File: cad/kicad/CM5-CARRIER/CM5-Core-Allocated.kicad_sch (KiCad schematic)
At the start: 7 parts, among them J501 RADXA CM5 U13-A MATE, J502 RADXA CM5 U13-B MATE, J503 RADXA CM5 J1 MATE, J510 CM5_POWER_SERVICE, J511 DEBUG_UART_3V3, J512 INTERNAL_USB_RECOVERY, J513 CM5_POWER_ENTRY

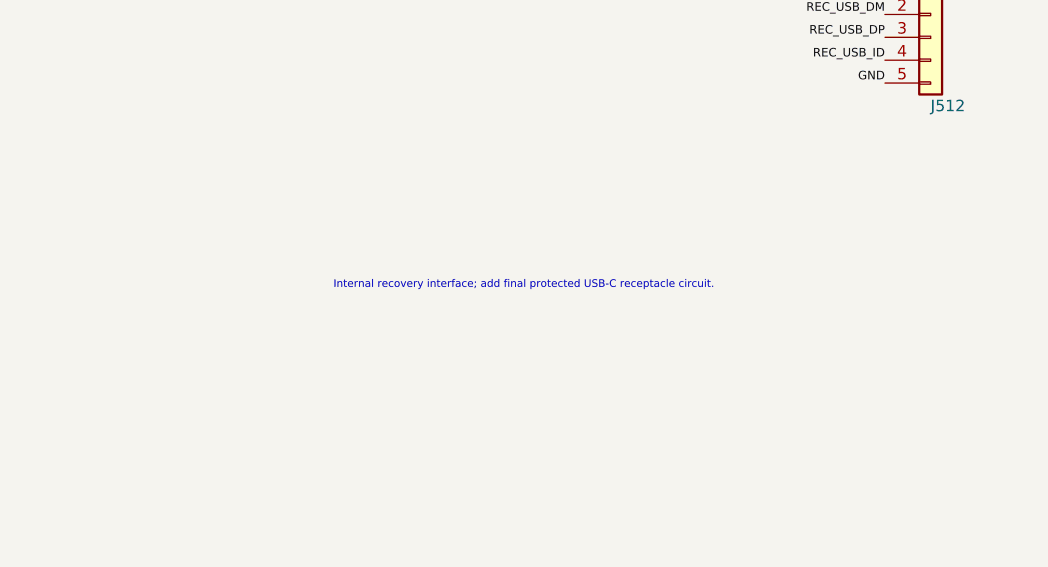
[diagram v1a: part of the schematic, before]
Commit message: Complete A1 detailed carrier and audio capture
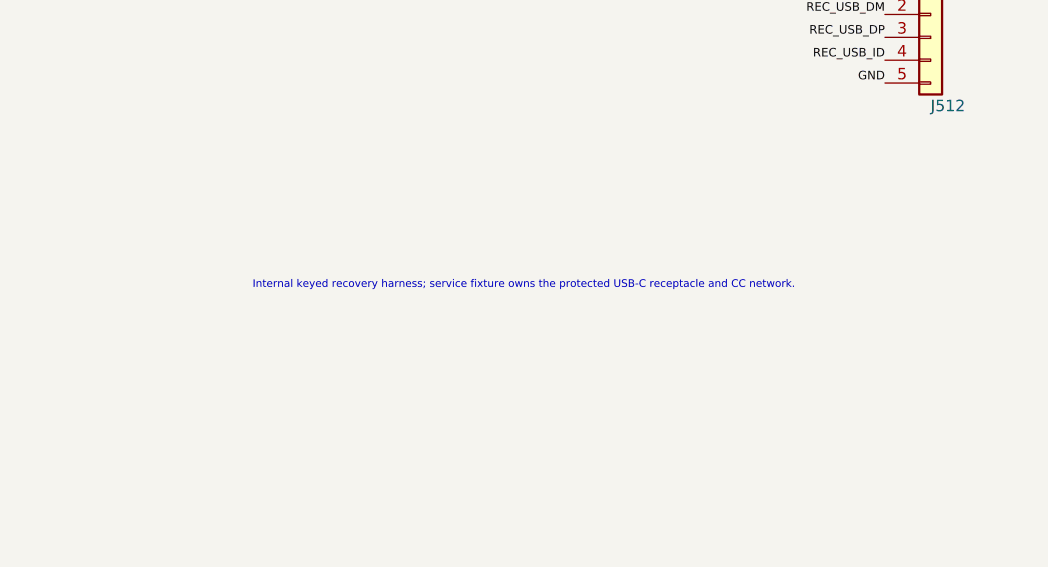
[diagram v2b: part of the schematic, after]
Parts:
- J510: footprint (none) -> Connector_JST:JST_GH_BM06B-GHS-TBT_1x06-1MP_P1.25mm_Vertical; MPN (none) -> BM06B-GHS-TBT(LF)(SN); Manufacturer (none) -> JST
- J511: footprint (none) -> Connector_JST:JST_GH_BM04B-GHS-TBT_1x04-1MP_P1.25mm_Vertical; MPN (none) -> BM04B-GHS-TBT(LF)(SN); Manufacturer (none) -> JST
- J512: footprint (none) -> Connector_JST:JST_GH_BM05B-GHS-TBT_1x05-1MP_P1.25mm_Vertical; MPN (none) -> BM05B-GHS-TBT(LF)(SN); Manufacturer (none) -> JST
- J513: footprint (none) -> Connector_Molex:Molex_Micro-Fit_3.0_43045-0812_2x04_P3.00mm_Vertical; MPN (none) -> 43045-0812; Manufacturer (none) -> Molex
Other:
- note added: "Internal keyed recovery harness; service fixture owns the protected USB-C receptacle and CC network."
- note removed: "Internal recovery interface; add final protected USB-C receptacle circuit."
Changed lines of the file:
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@@
+			)
+		)
+		(property "Footprint" "Connector_JST:JST_GH_BM06B-GHS-TBT_1x06-1MP_P1.25mm_Vertical"
+			(at 90.17 234.95 0.0000)
+			(effects
+				(font
+					(size 1.27 1.27)
+				)
+				(hide yes)
+			)
+		)
+		(property "Manufacturer" "JST"
+			(at 92.71 240.0299 0)
+			(effects
+				(font
+					(size 1.27 1.27)
+				)
+				(hide yes)
+			)
+		)
+		(property "MPN" "BM06B-GHS-TBT(LF)(SN)"
+			(at 92.71 240.0299 0)
+			(effects
+				(font
+					(size 1.27 1.27)
+				)
+				(hide yes)
 			)
 		)
@@
 			)
 		)
+		(property "Footprint" "Connector_JST:JST_GH_BM04B-GHS-TBT_1x04-1MP_P1.25mm_Vertical"
+			(at 214.63 232.41 0.0000)
+			(effects
+				(font
+					(size 1.27 1.27)
+				)
+				(hide yes)
+			)
+		)
+		(property "Manufacturer" "JST"
+			(at 217.17 237.4899 0)
+			(effects
+				(font
+					(size 1.27 1.27)
+				)
+				(hide yes)
+			)
+		)
+		(property "MPN" "BM04B-GHS-TBT(LF)(SN)"
+			(at 217.17 237.4899 0)
+			(effects
+				(font
+					(size 1.27 1.27)
+				)
+				(hide yes)
+			)
+		)
 		(pin "1"
 		)
@@
 			)
 		)
+		(property "Footprint" "Connector_JST:JST_GH_BM05B-GHS-TBT_1x05-1MP_P1.25mm_Vertical"
+			(at 330.2 232.41 0.0000)
+			(effects
+				(font
+					(size 1.27 1.27)
+				)
+				(hide yes)
+			)
+		)
+		(property "Manufacturer" "JST"
+			(at 332.74 237.4899 0)
+			(effects
+				(font
+					(size 1.27 1.27)
+				)
+				(hide yes)
+			)
+		)
+		(property "MPN" "BM05B-GHS-TBT(LF)(SN)"
+			(at 332.74 237.4899 0)
+			(effects
+				(font
+					(size 1.27 1.27)
+				)
+				(hide yes)
+			)
+		)
 		(pin "1"
 		)
@@
 			)
 		)
+		(property "Footprint" "Connector_Molex:Molex_Micro-Fit_3.0_43045-0812_2x04_P3.00mm_Vertical"
+			(at 469.9 232.41 0.0000)
+			(effects
+				(font
+					(size 1.27 1.27)
+				)
+				(hide yes)
+			)
+		)
+		(property "Manufacturer" "Molex"
+			(at 472.44 237.4899 0)
+			(effects
+				(font
+					(size 1.27 1.27)
+				)
+				(hide yes)
+			)
+		)
+		(property "MPN" "43045-0812"
+			(at 472.44 237.4899 0)
+			(effects
+				(font
+					(size 1.27 1.27)
+				)
+				(hide yes)
+			)
+		)
 		(pin "1"
 		)
@@
 		)
 	)
-	(text "Internal recovery interface; add final protected USB-C receptacle circuit."
+	(text "Internal keyed recovery harness; service fixture owns the protected USB-C receptacle and CC network."
 		(exclude_from_sim no)
 		(at 285 260 0.0000)

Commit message: Lock CM5 power and radio interfaces before routing
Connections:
- net HDMI_5V_OPTION renamed IO_5V0
- net SYS_5V15 renamed SYS_4V0
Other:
- note added: "Kelvin-sense SYS_4V0 at J501; 4.0 V follows the Radxa CM5 carrier design note."
- note added: "Pins 145/147 remain HDMI HEAC reserved. U13-B pin 106 receives the dedicated IO_5V0 rail."
- note removed: "Kelvin-sense SYS_5V15 at J501; final setpoint remains a release gate."
- note removed: "Pins 145/147 remain HDMI HEAC reserved. HDMI_5V_OPTION remains a controlled DNP/link decision."
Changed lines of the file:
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@@
 		)
 	)
-	(label "SYS_5V15"
+	(label "SYS_4V0"
 		(at 77.47 139.7 0.0000)
 		(effects
@@
 		)
 	)
-	(label "SYS_5V15"
+	(label "SYS_4V0"
 		(at 77.47 142.24 0.0000)
 		(effects
@@
 		)
 	)
-	(label "SYS_5V15"
+	(label "SYS_4V0"
 		(at 77.47 144.78 0.0000)
 		(effects
@@
 		)
 	)
-	(label "SYS_5V15"
+	(label "SYS_4V0"
 		(at 77.47 147.32 0.0000)
 		(effects
@@
 		)
 	)
-	(label "SYS_5V15"
+	(label "SYS_4V0"
 		(at 77.47 149.86 0.0000)
 		(effects
@@
 		)
 	)
-	(label "SYS_5V15"
+	(label "SYS_4V0"
 		(at 77.47 152.4 0.0000)
 		(effects
@@
 		)
 	)
-	(label "HDMI_5V_OPTION"
+	(label "IO_5V0"
 		(at 322.58 48.26 0.0000)
 		(effects
@@
 		)
 	)
-	(label "SYS_5V15"
+	(label "SYS_4V0"
 		(at 464.82 229.87 0.0000)
 		(effects
@@
 		)
 	)
-	(label "SYS_5V15"
+	(label "SYS_4V0"
 		(at 477.52 229.87 0.0000)
 		(effects
@@
 		)
 	)
-	(label "SYS_5V15"
+	(label "SYS_4V0"
 		(at 464.82 232.41 0.0000)
 		(effects
@@
 		)
 	)
-	(label "SYS_5V15"
+	(label "SYS_4V0"
 		(at 477.52 232.41 0.0000)
 		(effects
@@
 		)
 	)
-	(text "Kelvin-sense SYS_5V15 at J501; final setpoint remains a release gate."
+	(text "Kelvin-sense SYS_4V0 at J501; 4.0 V follows the Radxa CM5 carrier design note."
 		(exclude_from_sim no)
 		(at 420 260 0.0000)
@@
 		)
 	)
-	(text "Pins 145/147 remain HDMI HEAC reserved. HDMI_5V_OPTION remains a controlled DNP/link decision."
+	(text "Pins 145/147 remain HDMI HEAC reserved. U13-B pin 106 receives the dedicated IO_5V0 rail."
 		(exclude_from_sim no)
 		(at 45 348 0.0000)

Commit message: Audit schematic logic against controlled datasheets
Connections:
- net HDMI_HEAC_N: no longer names the net of J502.147 (HDMI0_TX_SBDN)
- net PCIE_UP_PERST_N renamed PCIE_UP_PERST_CMD_N
- net WAN1_LED2: no longer names the net of J501.15 (PHY1_LED2_Y)
- no-connect marks 148 -> 150
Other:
- note added: "76 / 76 contacts owned; 74 connected, 2 assigned NC, 0 duplicate physical-pin claims."
- note added: "Pin 145 reaches HDMI pin 14; pin 147 is assigned NC because HEAC/ARC is unused. U13-B pin 106 receives IO_5V0."
- note removed: "76 / 76 allocated contacts connected; 0 duplicate physical-pin claims."
- note removed: "Pins 145/147 remain HDMI HEAC reserved. U13-B pin 106 receives the dedicated IO_5V0 rail."

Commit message: Lock source-verified PCB mating geometry
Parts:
- J501: footprint Connector_Hirose_DF40:Hirose_DF40C-100DS-0.4V_2x50_P0.4mm -> CM5Carrier:Radxa_CM5_U33A_DF40C_100DS_OFFICIAL
- J502: footprint Connector_Hirose_DF40:Hirose_DF40C-100DS-0.4V_2x50_P0.4mm -> CM5Carrier:Radxa_CM5_U33B_DF40C_100DS_OFFICIAL
- J503: footprint Connector_Hirose_DF40:Hirose_DF40C-100DS-0.4V_2x50_P0.4mm -> CM5Carrier:Radxa_CM5_J24_DF40C_100DS_OFFICIAL
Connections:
- net GND: now also J501.201 (MODULE_MOUNT_GND_1), J501.202 (MODULE_MOUNT_GND_2), J501.203 (MODULE_MOUNT_GND_3), J501.204 (MODULE_MOUNT_GND_4)
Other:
- note added: "PCB lock: J501 and J502 share the U33 origin; J503 is +11.405, -25.415 mm at -90 degrees."
- note added: "U13-A: 100 contacts + official grounded module pads 201-204"
- note removed: "U13-A: 100 physical contacts"
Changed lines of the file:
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@@
 		(rev "A1")
 		(company "ProComm")
-		(comment 1 "Three 100-contact Hirose DF40C mates; all physical pin numbers follow CM5 V2.21")
+		(comment 1 "Three DF40C-100DS mates; pad geometry and relative placement come from Radxa IO V2.20")
 		(comment 2 "76 contacts are owned: 74 connected and 2 assigned no-connect; all other functions are no-connect")
-		(comment 3 "All connector grounds join the carrier ground plane; allocated GPIO domain is 3.3 V")
+		(comment 3 "U33-A includes the four official grounded CM5 mounting pads; allocated GPIO domain is 3.3 V")
 		(comment 4 "DETAILED CAPTURE BASELINE - verify CM5 voltage limits before release")
 	)
@@
 			)
 		)
-		(property "Footprint" "Connector_Hirose_DF40:Hirose_DF40C-100DS-0.4V_2x50_P0.4mm"
+		(property "Footprint" "CM5Carrier:Radxa_CM5_U33A_DF40C_100DS_OFFICIAL"
 			(at 105.41 105.41 0.0000)
 			(effects
@@
 		(pin "100"
 		)
+		(pin "201"
+		)
+		(pin "202"
+		)
+		(pin "203"
+		)
+		(pin "204"
+		)
 		(instances
 			(project "CM5-Core-Allocated"
-				(path "/39dba5e7-0a78-5371-8db7-ef167c3abd72"
+				(path "/e76c176a-1953-5024-84a9-8e57eaed08fb"
 					(reference "J501")
 					(unit 1)
@@
 			)
 		)
-		(property "Footprint" "Connector_Hirose_DF40:Hirose_DF40C-100DS-0.4V_2x50_P0.4mm"
+		(property "Footprint" "CM5Carrier:Radxa_CM5_U33B_DF40C_100DS_OFFICIAL"
 			(at 294.64 105.41 0.0000)
 			(effects
@@
 		(instances
 			(project "CM5-Core-Allocated"
-				(path "/39dba5e7-0a78-5371-8db7-ef167c3abd72"
+				(path "/e76c176a-1953-5024-84a9-8e57eaed08fb"
 					(reference "J502")
 					(unit 1)
@@
 			)
 		)
-		(property "Footprint" "Connector_Hirose_DF40:Hirose_DF40C-100DS-0.4V_2x50_P0.4mm"
+		(property "Footprint" "CM5Carrier:Radxa_CM5_J24_DF40C_100DS_OFFICIAL"
 			(at 485.14 105.41 0.0000)
 			(effects
@@
 		(instances
 			(project "CM5-Core-Allocated"
-				(path "/39dba5e7-0a78-5371-8db7-ef167c3abd72"
+				(path "/e76c176a-1953-5024-84a9-8e57eaed08fb"
 					(reference "J503")
 					(unit 1)
@@
 		(instances
 			(project "CM5-Core-Allocated"
-				(path "/39dba5e7-0a78-5371-8db7-ef167c3abd72"
+				(path "/e76c176a-1953-5024-84a9-8e57eaed08fb"
 					(reference "J510")
 					(unit 1)
@@
 		(instances
 			(project "CM5-Core-Allocated"
-				(path "/39dba5e7-0a78-5371-8db7-ef167c3abd72"
+				(path "/e76c176a-1953-5024-84a9-8e57eaed08fb"
 					(reference "J511")
 					(unit 1)
@@
 		(instances
 			(project "CM5-Core-Allocated"
-				(path "/39dba5e7-0a78-5371-8db7-ef167c3abd72"
+				(path "/e76c176a-1953-5024-84a9-8e57eaed08fb"
 					(reference "J512")
 					(unit 1)
@@
 		(instances
 			(project "CM5-Core-Allocated"
-				(path "/39dba5e7-0a78-5371-8db7-ef167c3abd72"
+				(path "/e76c176a-1953-5024-84a9-8e57eaed08fb"
 					(reference "J513")
 					(unit 1)
@@
 		)
 	)
+	(global_label "GND"
+		(shape bidirectional)
+		(at 77.47 171.45 0.0000)
+		(effects
+			(font
+				(size 0.62 0.62)
+			)
+			(justify right bottom)
+		)
+	)
+	(global_label "GND"
+		(shape bidirectional)
+		(at 133.35 171.45 0.0000)
+		(effects
+			(font
+				(size 0.62 0.62)
+			)
+			(justify left bottom)
+		)
+	)
+	(global_label "GND"
+		(shape bidirectional)
+		(at 77.47 173.99 0.0000)
+		(effects
+			(font
+				(size 0.62 0.62)
+			)
+			(justify right bottom)
+		)
+	)
+	(global_label "GND"
+		(shape bidirectional)
+		(at 133.35 173.99 0.0000)
+		(effects
+			(font
+				(size 0.62 0.62)
+			)
+			(justify left bottom)
+		)
+	)
 	(global_label "REC_USB_ID"
 		(shape bidirectional)
@@
 		)
 	)
-	(text "U13-A: 100 physical contacts"
+	(text "U13-A: 100 contacts + official grounded module pads 201-204"
 		(exclude_from_sim no)
-		(at 77 174 0.0000)
+		(at 77 178 0.0000)
 		(effects
 			(font
@@
 	(text "U13-B: 100 physical contacts"
 		(exclude_from_sim no)
-		(at 267 174 0.0000)
+		(at 267 178 0.0000)
 		(effects
 			(font
@@
 	(text "J1: 100 physical contacts"
 		(exclude_from_sim no)
-		(at 457 174 0.0000)
+		(at 457 178 0.0000)
 		(effects
 			(font
@@
 			)
 		)
+	)
+	(text "PCB lock: J501 and J502 share the U33 origin; J503 is +11.405, -25.415 mm at -90 degrees."
+		(exclude_from_sim no)
+		(at 420 270 0.0000)
+		(effects
+			(font
+				(size 0.82 0.82)
+			)
+		)
